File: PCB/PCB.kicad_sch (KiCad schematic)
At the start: 211 parts, among them J1 Conn_01x04, J2 USB_C_Receptacle_USB2.0_16P, J3 Conn_01x05, SW1 MX_SW_HS, SW10 MX_SW_HS, SW11 MX_SW_HS, SW12 MX_SW_HS, SW13 MX_SW_HS, SW15 MX_SW_HS, SW16 MX_SW_HS, SW17 MX_SW_HS, SW18 MX_SW_HS, SW19 MX_SW_HS, SW2 MX_SW_HS, SW20 MX_SW_HS, SW21 MX_SW_HS, SW22 MX_SW_HS, SW23 MX_SW_HS, SW24 MX_SW_HS, SW25 MX_SW_HS, SW26 MX_SW_HS, SW27 MX_SW_HS, SW28 MX_SW_HS, SW29 MX_SW_HS, SW3 MX_SW_HS, SW30 MX_SW_HS, SW31 MX_SW_HS, SW32 MX_SW_HS, SW33 MX_SW_HS, SW34 MX_SW_HS, SW35 MX_SW_HS, SW36 MX_SW_HS, SW37 MX_SW_HS, SW38 MX_SW_HS, SW39 MX_SW_HS, SW4 MX_SW_HS, SW40 MX_SW_HS, SW41 MX_SW_HS, SW42 MX_SW_HS, SW43 MX_SW_HS, SW44 MX_SW_HS, SW45 MX_SW_HS, SW46 MX_SW_HS, SW47 MX_SW_HS, SW48 MX_SW_HS, SW49 MX_SW_HS, SW5 MX_SW_HS, SW50 MX_SW_HS, SW51 MX_SW_HS, SW52 MX_SW_HS, SW53 MX_SW_HS, SW54 MX_SW_HS, SW55 MX_SW_HS, SW56 MX_SW_HS, SW57 MX_SW_HS, SW58 MX_SW_HS, SW59 MX_SW_HS, SW6 MX_SW_HS, SW60 MX_SW_HS, SW61 MX_SW_HS, SW62 MX_SW_HS, SW63 MX_SW_HS, SW64 MX_SW_HS, SW65 MX_SW_HS, SW66 MX_SW_HS, SW67 MX_SW_HS, SW68 MX_SW_HS, SW69 MX_SW_HS, SW7 MX_SW_HS, SW70 MX_SW_HS, SW71 MX_SW_HS, SW72 MX_SW_HS, SW73 MX_SW_HS, SW74 MX_SW_HS, SW75 MX_SW_HS, SW76 MX_SW_HS, SW77 MX_SW_HS, SW78 MX_SW_HS, SW79 MX_SW_HS, SW8 MX_SW_HS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

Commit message: idk update
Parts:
- added C11, C12, C13, C5: 100n, Capacitor_SMD:C_0402_1005Metric, symbol Device:C_Small
- renumbered C9 to C10, C10 to C14, C11 to C15, C12 to C16, C5 to C6, C6 to C7, C7 to C8, C8 to C9, D15 to D14, D16 to D15, D17 to D16, D18 to D17, D19 to D18, D20 to D19, D21 to D20, D22 to D21, D23 to D22, D24 to D23, D25 to D24, D26 to D25, D27 to D26, D28 to D27, D29 to D28, D30 to D29, D31 to D30, D32 to D31, D33 to D32, D34 to D33, D35 to D34, D36 to D35, D37 to D36, D38 to D37, D39 to D38, D40 to D39, D41 to D40, D42 to D41, D43 to D42, D44 to D43, D45 to D44, D46 to D45, D47 to D46, D48 to D47, D49 to D48, D50 to D49, D51 to D50, D52 to D51, D53 to D52, D54 to D53, D55 to D54, D56 to D55, D57 to D56, D58 to D57, D59 to D58, D60 to D59, D61 to D60, D62 to D61, D63 to D62, D64 to D63, D65 to D64, D66 to D65, D67 to D66, D68 to D67, D69 to D68, D70 to D69, D71 to D70, D72 to D71, D73 to D72, D74 to D73, D75 to D74, D76 to D75, D77 to D76, D78 to D77, D79 to D78, D80 to D79, D81 to D80, D82 to D81, D83 to D82, D84 to D83, D85 to D84, D86 to D85, D87 to D86, D88 to D87, S5 to S4, S4 to S5, SW15 to SW14, SW16 to SW15, SW17 to SW16, SW18 to SW17, SW19 to SW18, SW20 to SW19, SW21 to SW20, SW22 to SW21, SW23 to SW22, SW24 to SW23, SW25 to SW24, SW26 to SW25, SW27 to SW26, SW28 to SW27, SW29 to SW28, SW30 to SW29, SW31 to SW30, SW32 to SW31, SW33 to SW32, SW34 to SW33, SW35 to SW34, SW36 to SW35, SW37 to SW36, SW38 to SW37, SW39 to SW38, SW40 to SW39, SW41 to SW40, SW42 to SW41, SW43 to SW42, SW44 to SW43, SW45 to SW44, SW46 to SW45, SW47 to SW46, SW48 to SW47, SW49 to SW48, SW50 to SW49, SW51 to SW50, SW52 to SW51, SW53 to SW52, SW54 to SW53, SW55 to SW54, SW56 to SW55, SW57 to SW56, SW58 to SW57, SW59 to SW58, SW60 to SW59, SW61 to SW60, SW62 to SW61, SW63 to SW62, SW64 to SW63, SW65 to SW64, SW66 to SW65, SW67 to SW66, SW68 to SW67, SW69 to SW68, SW70 to SW69, SW71 to SW70, SW72 to SW71, SW73 to SW72, SW74 to SW73, SW75 to SW74, SW76 to SW75, SW77 to SW76, SW78 to SW77, SW79 to SW78, SW80 to SW79, SW81 to SW80, SW82 to SW81, SW83 to SW82, SW84 to SW83, SW85 to SW84, SW86 to SW85, SW87 to SW86, SW88 to SW87
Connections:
- net +1V1: now also U3.23 (DVDD), U3.45 (VREG_VOUT), U3.50 (DVDD), C5.1; no longer U3.43 (ADC_AVDD), U3.48 (USB_VDD)
- net +3V3: now also U3.43 (ADC_AVDD), U3.48 (USB_VDD), C11.1, C12.1, C13.1; no longer U3.23 (DVDD), U3.45 (VREG_VOUT), U3.50 (DVDD)
- net D+: now also R8.1; no longer R7.1
- net D-: now also R7.1; no longer R8.1
- net GND: now also C11.2, C12.2, C13.2, C5.2
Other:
- moved on the sheet: C3, C4

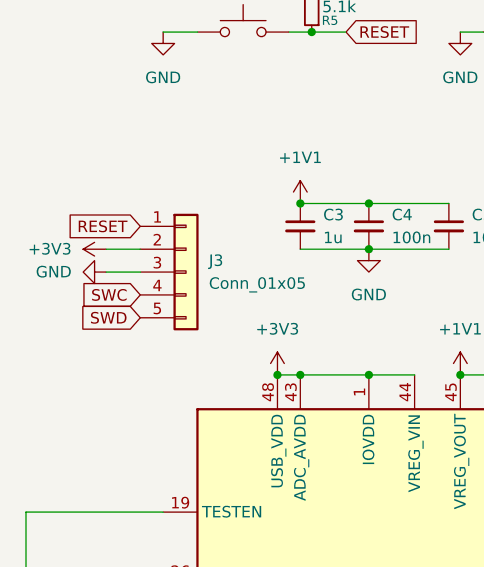
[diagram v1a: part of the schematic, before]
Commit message: finished routing mcu and everything besides switch matrix. have to fix usb port
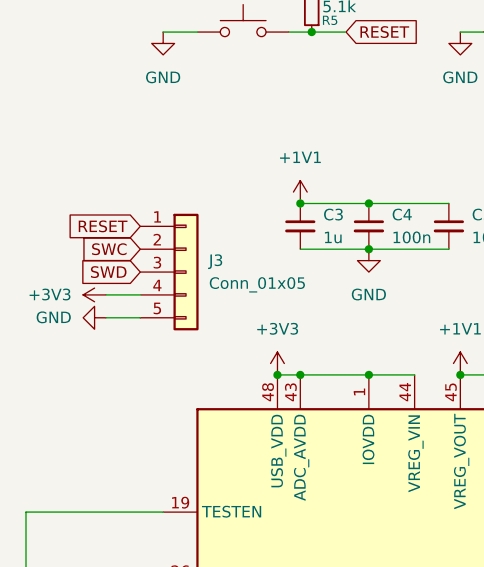
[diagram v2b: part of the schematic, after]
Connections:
- net +3V3: now also J3.4 (Pin_4); no longer J3.2 (Pin_2)
- net GND: now also J3.5 (Pin_5); no longer J3.3 (Pin_3)
- net SWC: now also J3.2 (Pin_2); no longer J3.4 (Pin_4)
- net SWD: now also J3.3 (Pin_3); no longer J3.5 (Pin_5)
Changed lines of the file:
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@@
 	(wire
 		(pts
-			(xy 21.59 135.89) (xy 25.4 135.89)
+			(xy 21.59 140.97) (xy 25.4 140.97)
 		)
 		(stroke
@@
 	(wire
 		(pts
-			(xy 21.59 138.43) (xy 25.4 138.43)
+			(xy 21.59 143.51) (xy 25.4 143.51)
 		)
 		(stroke
@@
 	(global_label "SWC"
 		(shape input)
-		(at 25.4 140.97 180)
+		(at 25.4 135.89 180)
 		(fields_autoplaced yes)
 		(effects
@@
 		)
 		(property "Intersheetrefs" "${INTERSHEET_REFS}"
-			(at 18.4839 140.97 0)
+			(at 18.4839 135.89 0)
 			(hide yes)
 			(show_name no)
@@
 	(global_label "SWD"
 		(shape input)
-		(at 25.4 143.51 180)
+		(at 25.4 138.43 180)
 		(fields_autoplaced yes)
 		(effects
@@
 		)
 		(property "Intersheetrefs" "${INTERSHEET_REFS}"
-			(at 18.4839 143.51 0)
+			(at 18.4839 138.43 0)
 			(hide yes)
 			(show_name no)
@@
 	(symbol
 		(lib_id "power:+3V3")
-		(at 21.59 135.89 90)
+		(at 21.59 140.97 90)
 		(unit 1)
 		(body_style 1)
@@
 		(fields_autoplaced yes)
 		(property "Reference" "#PWR018"
-			(at 25.4 135.89 0)
+			(at 25.4 140.97 0)
 			(hide yes)
 			(show_name no)
@@
 		)
 		(property "Value" "+3V3"
-			(at 17.78 135.8899 90)
+			(at 17.78 140.9699 90)
 			(show_name no)
 			(do_not_autoplace no)
@@
 		)
 		(property "Footprint" ""
-			(at 21.59 135.89 0)
+			(at 21.59 140.97 0)
 			(hide yes)
 			(show_name no)
@@
 		)
 		(property "Datasheet" ""
-			(at 21.59 135.89 0)
+			(at 21.59 140.97 0)
 			(hide yes)
 			(show_name no)
@@
 		)
 		(property "Description" "Power symbol creates a global label with name \"+3V3\""
-			(at 21.59 135.89 0)
+			(at 21.59 140.97 0)
 			(hide yes)
 			(show_name no)
@@
 	(symbol
 		(lib_id "power:GND")
-		(at 21.59 138.43 270)
+		(at 21.59 143.51 270)
 		(unit 1)
 		(body_style 1)
@@
 		(fields_autoplaced yes)
 		(property "Reference" "#PWR021"
-			(at 15.24 138.43 0)
+			(at 15.24 143.51 0)
 			(hide yes)
 			(show_name no)
@@
 		)
 		(property "Value" "GND"
-			(at 17.78 138.4299 90)
+			(at 17.78 143.5099 90)
 			(show_name no)
 			(do_not_autoplace no)
@@
 		)
 		(property "Footprint" ""
-			(at 21.59 138.43 0)
+			(at 21.59 143.51 0)
 			(hide yes)
 			(show_name no)
@@
 		)
 		(property "Datasheet" ""
-			(at 21.59 138.43 0)
+			(at 21.59 143.51 0)
 			(hide yes)
 			(show_name no)
@@
 		)
 		(property "Description" "Power symbol creates a global label with name \"GND\" , ground"
-			(at 21.59 138.43 0)
+			(at 21.59 143.51 0)
 			(hide yes)
 			(show_name no)

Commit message: added title block
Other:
- company: (none) -> Saurya Shrestha
- title: (none) -> TKL Keyboard
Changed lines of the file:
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@@
 	(generator_version "10.0")
 	(paper "A3")
+	(title_block
+		(title "TKL Keyboard")
+		(date "2026-10-25")
+		(rev "1")
+		(company "Saurya Shrestha")
+	)
 	(junction
 		(at 91.44 130.81)
